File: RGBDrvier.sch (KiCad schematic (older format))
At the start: 9 parts, among them U2601 PCA9745BTWJ

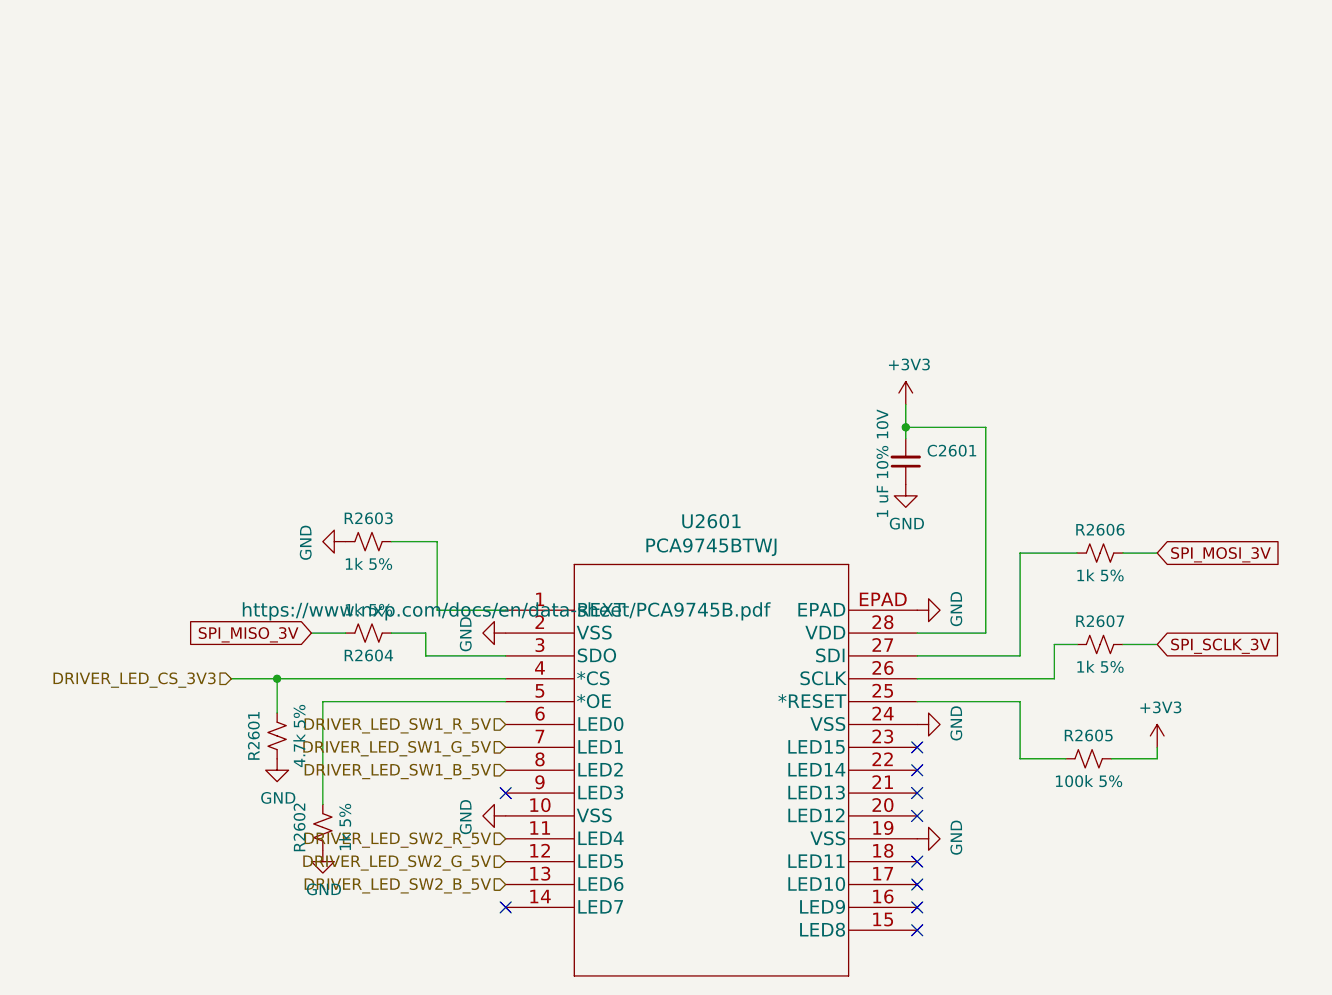
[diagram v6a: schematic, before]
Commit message: Remove resistor for SPI MOSI, MISO, and CS for LED Driver
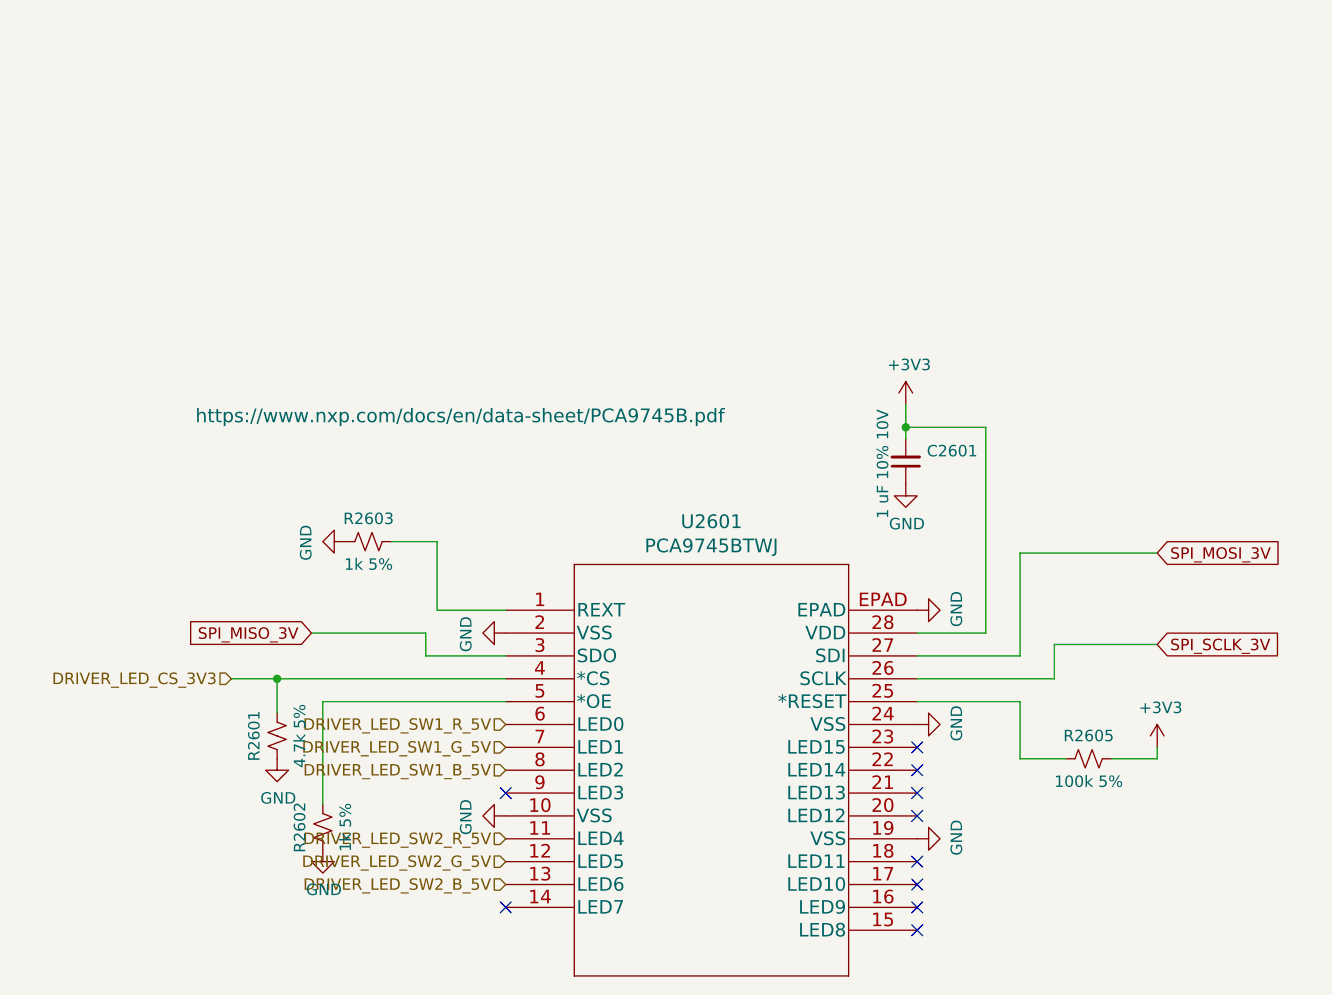
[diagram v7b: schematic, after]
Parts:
- removed R2604, R2606, R2607: 1k 5%, Resistor_SMD:R_0805_2012Metric_Pad1.20x1.40mm_HandSolder, symbol Device:R_Small_US
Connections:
- net SPI_MISO_3V: now also U2601.3 (SDO)
- net SPI_MOSI_3V: now also U2601.27 (SDI)
- net SPI_SCLK_3V: now also U2601.26 (SCLK)
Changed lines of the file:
@@
 $EndDescr
-$Comp
-L Device:R_Small_US R2604
-U 1 1 61A3FADF
-P 4450 3300
-F 0 "R2604" V 4550 3300 50  0000 C CNN
-F 1 "1k 5%" V 4350 3300 50  0000 C CNN
-F 2 "Resistor_SMD:R_0805_2012Metric_Pad1.20x1.40mm_HandSolder" H 4450 3300 50  0001 C CNN
-F 3 "https://www.seielect.com/catalog/sei-rmcf_rmcp.pdf" H 4450 3300 50  0001 C CNN
-F 4 "RMCF0805JT1K00CT-ND" H 4450 3300 50  0001 C CNN "Digikey PN"
-F 5 "Stackpole Electronics Inc" H 4450 3300 50  0001 C CNN "MFG"
-F 6 "RMCF0805JT1K00" H 4450 3300 50  0001 C CNN "MFG #"
-	1    4450 3300
-	0    1    1    0
-$EndComp
 $Comp
 L Device:R_Small_US R2602
@@
 $EndComp
 $Comp
-L Device:R_Small_US R2607
-U 1 1 61A429FE
-P 7650 3350
-F 0 "R2607" V 7550 3350 50  0000 C CNN
-F 1 "1k 5%" V 7750 3350 50  0000 C CNN
-F 2 "Resistor_SMD:R_0805_2012Metric_Pad1.20x1.40mm_HandSolder" H 7650 3350 50  0001 C CNN
-F 3 "https://www.seielect.com/catalog/sei-rmcf_rmcp.pdf" H 7650 3350 50  0001 C CNN
-F 4 "RMCF0805JT1K00CT-ND" H 7650 3350 50  0001 C CNN "Digikey PN"
-F 5 "Stackpole Electronics Inc" H 7650 3350 50  0001 C CNN "MFG"
-F 6 "RMCF0805JT1K00" H 7650 3350 50  0001 C CNN "MFG #"
-	1    7650 3350
-	0    1    1    0
-$EndComp
-$Comp
 L Device:R_Small_US R2601
 U 1 1 61A3D9CE
@@
 Text HLabel 5050 3900 0    50   Input ~ 0
 DRIVER_LED_SW1_B_5V
-$Comp
-L Device:R_Small_US R2606
-U 1 1 61A5BA43
-P 7650 2950
-F 0 "R2606" V 7550 2950 50  0000 C CNN
-F 1 "1k 5%" V 7750 2950 50  0000 C CNN
-F 2 "Resistor_SMD:R_0805_2012Metric_Pad1.20x1.40mm_HandSolder" H 7650 2950 50  0001 C CNN
-F 3 "https://www.seielect.com/catalog/sei-rmcf_rmcp.pdf" H 7650 2950 50  0001 C CNN
-F 4 "RMCF0805JT1K00CT-ND" H 7650 2950 50  0001 C CNN "Digikey PN"
-F 5 "Stackpole Electronics Inc" H 7650 2950 50  0001 C CNN "MFG"
-F 6 "RMCF0805JT1K00" H 7650 2950 50  0001 C CNN "MFG #"
-	1    7650 2950
-	0    1    1    0
-$EndComp
 Text GLabel 7900 3350 2    50   Input ~ 0
 SPI_SCLK_3V
@@
 	7450 3500 7450 3350
 Wire Wire Line
-	7450 3350 7550 3350
-Wire Wire Line
 	6850 3500 7450 3500
-Wire Wire Line
-	7300 2950 7550 2950
-Wire Wire Line
-	7900 2950 7750 2950
-Wire Wire Line
-	7750 3350 7900 3350
 NoConn ~ 6850 3800
 NoConn ~ 6850 3900
@@
 SPI_MISO_3V
 Wire Wire Line
-	4200 3300 4350 3300
-Wire Wire Line
-	4550 3300 4700 3300
-Wire Wire Line
 	4700 3300 4700 3400
 $Comp
@@
 F 1 "PCA9745BTWJ" H 5950 3481 60  0000 C CNN
 F 2 "Macro Keyboard:PCA9745BTWJ" H 5950 3440 60  0001 C CNN
-F 3 "https://www.nxp.com/docs/en/data-sheet/PCA9745B.pdf" H 5050 3200 60  0000 C CNN
+F 3 "https://www.nxp.com/docs/en/data-sheet/PCA9745B.pdf" H 4850 4050 60  0000 C CNN
 F 4 "568-14156-1-ND" H 5050 3200 50  0001 C CNN "Digikey PN"
 F 5 "NXP USA Inc." H 5050 3200 50  0001 C CNN "MFG"
@@
 Text HLabel 5050 4200 0    50   Input ~ 0
 DRIVER_LED_SW2_R_5V
+Wire Wire Line
+	4700 3300 4200 3300
+Wire Wire Line
+	7300 2950 7900 2950
+Wire Wire Line
+	7450 3350 7900 3350
 $EndSCHEMATC
